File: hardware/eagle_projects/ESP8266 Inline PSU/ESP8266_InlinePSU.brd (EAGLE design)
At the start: 100 x 80 mm, 1 part

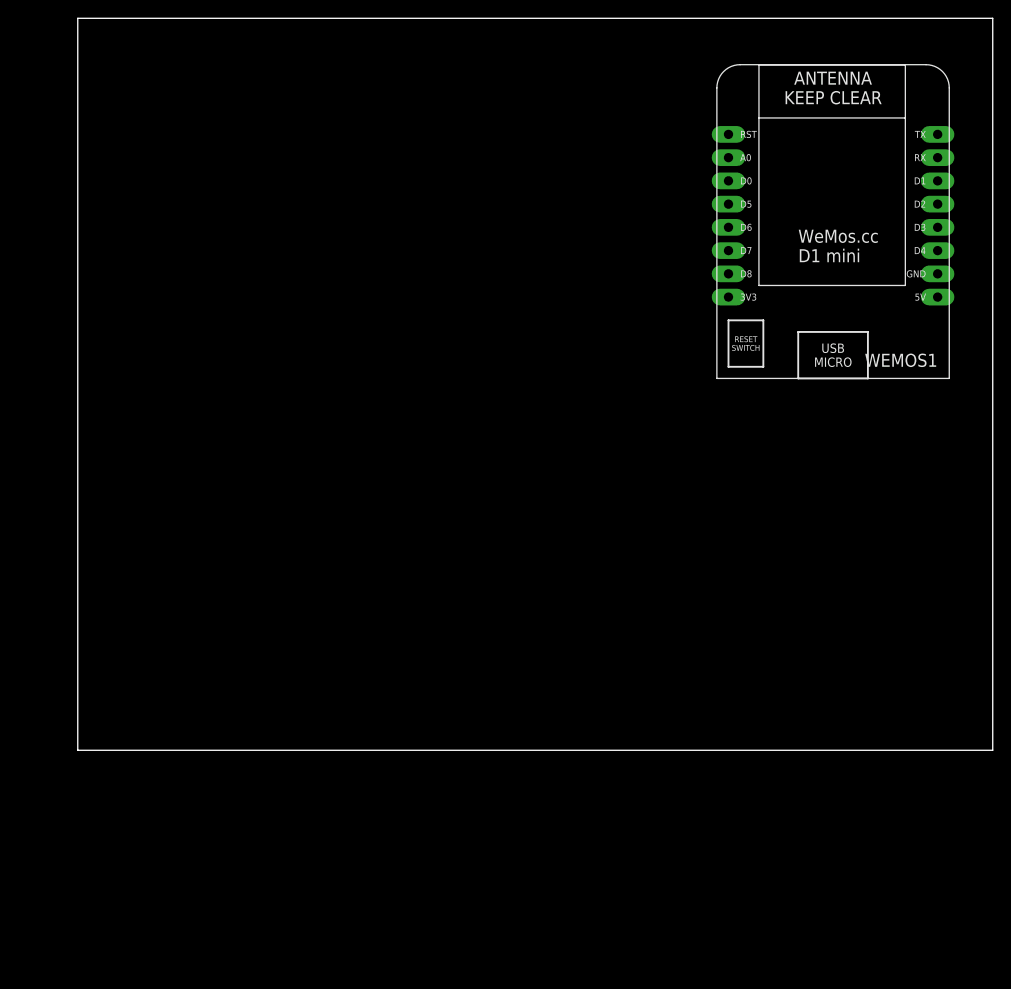
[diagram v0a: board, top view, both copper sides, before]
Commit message: Beginning build process for wireless inline PSU and modifications of PSU
Signed-off-by: Braden Licastro <blicastro@live.com>
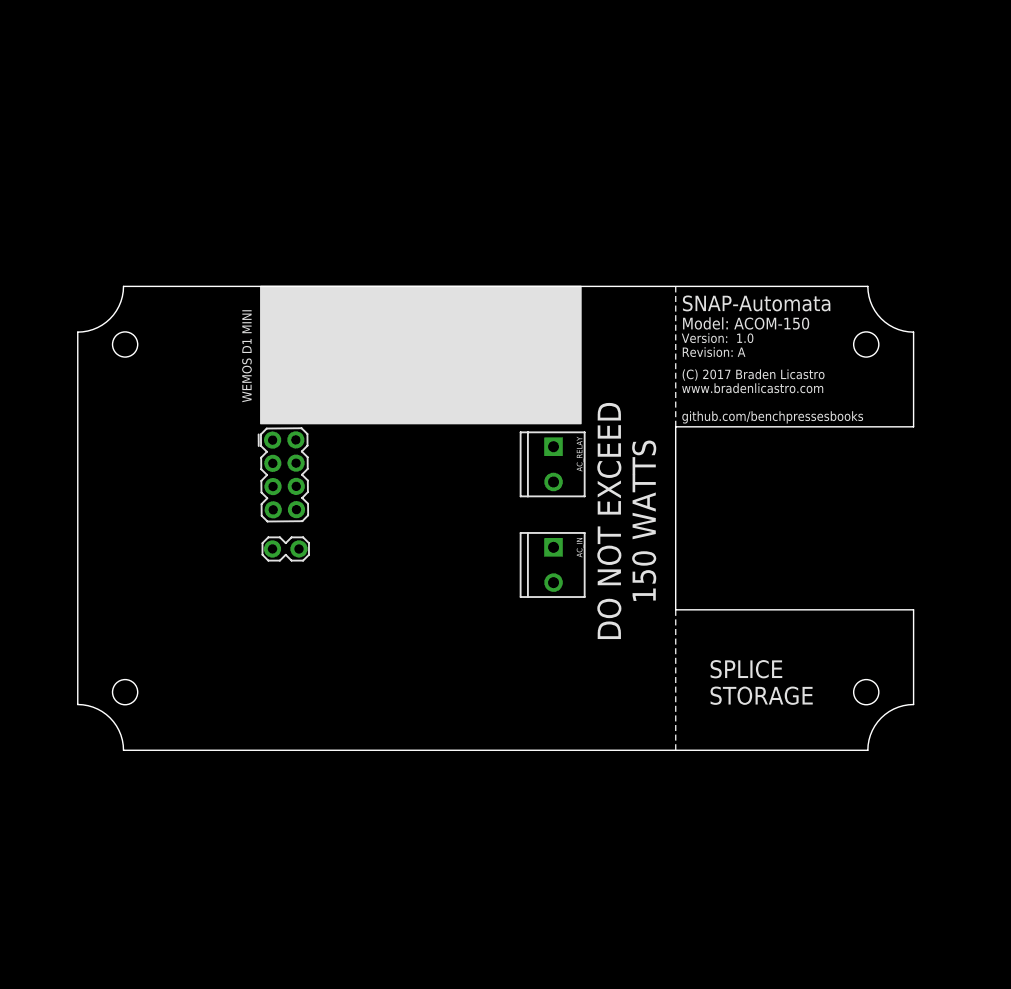
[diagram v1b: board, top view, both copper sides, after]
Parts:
- removed WEMOS1: (no value), esp8266modules:WEMOS-D1-MINI
- added AC_IN, AC_RELAY: (no value), SparkFun-Connectors:SCREWTERMINAL-3.5MM-2_LOCK
- added OVRRD: (no value), SparkFun-Connectors:1X02_LOCK
- added REMOTE_INFC: (no value), SparkFun-Connectors:2X4
- added WEMOS_INFC: (no value), SparkFun-Connectors:2X8
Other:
- board size 100 x 80 mm -> 91.3 x 50.7 mm
- board text added: "(C) 2017 Braden Licastro www.bradenlicastro.com github.com/benchpressesbooks"
- board text added: "DO NOT EXCEED 150 WATTS"
- board text added: "Model: ACOM-150"
- board text added: "SNAP-Automata"
- board text added: "SPLICE STORAGE"
- board text added: "Version: 1.0 Revision: A"
- board text added: "WEMOS D1 MINI"

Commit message: Completed more work on hardware design. Broke out sections of sensitive code, optimised existing code. Hacked new device for use and built new firmware. Updated test firmware for deployment on multiple ESP devices.
Signed-off-by: Braden Licastro <blicastro@live.com>
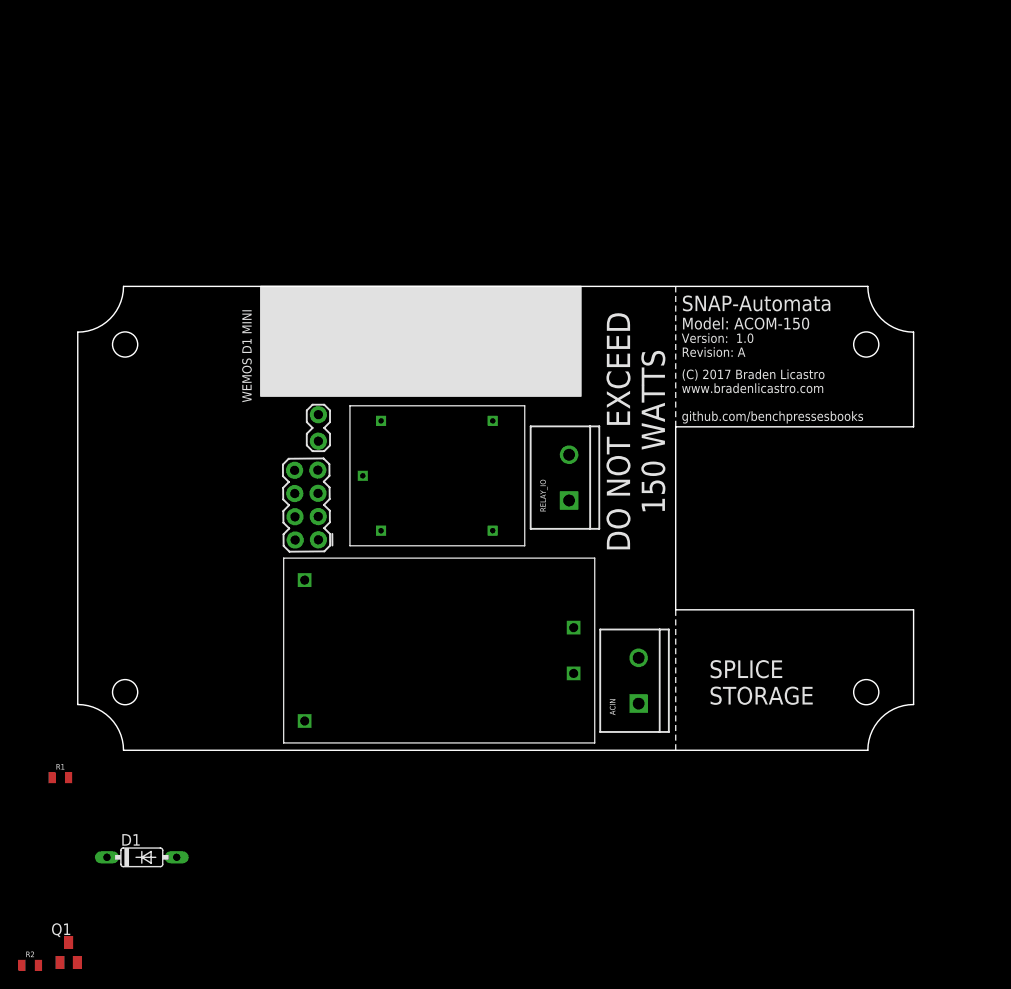
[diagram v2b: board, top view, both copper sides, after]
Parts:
- removed AC_IN, AC_RELAY: (no value), SparkFun-Connectors:SCREWTERMINAL-3.5MM-2_LOCK
- removed WEMOS_INFC: (no value), SparkFun-Connectors:2X8
- added ACIN, RELAY_IO: (no value), SparkFun-Connectors:SCREWTERMINAL-5MM-2
- added D1: 1N4148DO35-7, diode:DO35-7
- added HKLP1: HKLPM01, bl_components:HKLPM01
- added Q1: (no value), semicon-smd-ipc:SOT23
- added R1, R2: (no value), SparkFun-Resistors:0805
- added U$1: SRD-05VDC-SL-CTH, bl_components:SRD-05VDC-SL-C
- added WEMOS_INFC1: (no value), SparkFun-Connectors:2X8
- moved OVRRD 14.7 mm to (26.3, 36.5), turned to 270 degrees
- moved REMOTE_INFC 4.08 mm to (25.0, 26.8), turned to 90.5 degrees
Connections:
- new net N$1: ACIN.2, HKLP1.P$1
- new net N$10: Q1.1, R2.2
- new net N$11: R2.1, WEMOS_INFC1.11
- new net N$2: ACIN.1, HKLP1.P$2
- new net N$3: D1.C, HKLP1.P$4, REMOTE_INFC.1, U$1.P$3, WEMOS_INFC1.1
- new net N$4: OVRRD.1, REMOTE_INFC.2, WEMOS_INFC1.2
- new net N$5: HKLP1.P$3, Q1.2, R1.2, REMOTE_INFC.3, WEMOS_INFC1.3
- new net N$6: RELAY_IO.1, U$1.P$1
- new net N$7: RELAY_IO.2, U$1.P$4
- new net N$8: D1.A, Q1.3, U$1.P$5
- new net N$9: OVRRD.2, R1.1, WEMOS_INFC1.9
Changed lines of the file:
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@@
 <?xml version="1.0" encoding="utf-8"?>
 <!DOCTYPE eagle SYSTEM "eagle.dtd">
-<eagle version="8.4.0">
+<eagle version="8.4.3">
 <drawing>
 <settings>
@@
 <setting verticaltext="up"/>
 </settings>
-<grid distance="1" unitdist="mm" unit="mm" style="lines" multiple="1" display="yes" altdistance="5" altunitdist="mil" altunit="mil"/>
+<grid distance="100" unitdist="mic" unit="mm" style="lines" multiple="1" display="yes" altdistance="5" altunitdist="mil" altunit="mm"/>
 <layers>
 <layer number="1" name="Top" color="4" fill="1" visible="yes" active="yes"/>
@@
 <vertex x="20" y="50.7"/>
 <vertex x="55" y="50.7"/>
-<vertex x="55" y="35.7"/>
-<vertex x="20" y="35.7"/>
+<vertex x="55" y="38.7"/>
+<vertex x="20" y="38.7"/>
 </polygon>
 <text x="19" y="38" size="1.016" layer="21" rot="R90">WEMOS D1 MINI</text>
@@
 www.bradenlicastro.com
 github.com/benchpressesbooks</text>
-<text x="60" y="25" size="2.54" layer="21" rot="R270" align="center">DO NOT EXCEED
+<text x="61" y="34.8" size="2.54" layer="21" rot="R270" align="center">DO NOT EXCEED
 150 WATTS</text>
 </plain>
@@
 <param name="dpMaxLengthDifference" value="10mm"/>
 <param name="dpGapFactor" value="2.5"/>
+<param name="checkAngle" value="0"/>
 <param name="checkFont" value="1"/>
 <param name="checkRestrict" value="0"/>
@@
 </autorouter>
 <elements>
-<element name="WEMOS_INFC" library="SparkFun-Connectors" library_urn="urn:adsk.eagle:library:513" package="2X8" package3d_urn="urn:adsk.eagle:package:38152/1" value="" x="28.888240625" y="46.80739375" smashed="yes">
-<attribute name="VALUE" x="27.618240625" y="44.39439375" size="0.6096" layer="27" font="vector" ratio="20"/>
-</element>
-<element name="REMOTE_INFC" library="SparkFun-Connectors" library_urn="urn:adsk.eagle:library:513" package="2X4" package3d_urn="urn:adsk.eagle:package:38103/1" value="" x="22.6" y="30.1" smashed="yes" rot="R270.5">
-<attribute name="VALUE" x="18.8728125" y="35.14766875" size="0.6096" layer="27" font="vector" ratio="20" rot="R270.5"/>
-</element>
-<element name="OVRRD" library="SparkFun-Connectors" library_urn="urn:adsk.eagle:library:513" package="1X02_LOCK" package3d_urn="urn:adsk.eagle:package:38045/1" value="" x="24" y="22" smashed="yes" rot="R180">
-<attribute name="VALUE" x="25.27" y="24.032" size="0.6096" layer="27" font="vector" ratio="20" rot="R180"/>
-</element>
-<element name="AC_IN" library="SparkFun-Connectors" library_urn="urn:adsk.eagle:library:513" package="SCREWTERMINAL-3.5MM-2_LOCK" package3d_urn="urn:adsk.eagle:package:38049/1" value="" x="52" y="22" rot="R270">
-<attribute name="PROD_ID" value="CONN-08399" x="52" y="22" size="1.016" layer="27" rot="R270" display="off"/>
-</element>
-<element name="AC_RELAY" library="SparkFun-Connectors" library_urn="urn:adsk.eagle:library:513" package="SCREWTERMINAL-3.5MM-2_LOCK" package3d_urn="urn:adsk.eagle:package:38049/1" value="" x="52" y="33" rot="R270">
-<attribute name="PROD_ID" value="CONN-08399" x="52" y="33" size="1.016" layer="27" rot="R270" display="off"/>
+<element name="REMOTE_INFC" library="SparkFun-Connectors" library_urn="urn:adsk.eagle:library:513" package="2X4" package3d_urn="urn:adsk.eagle:package:38103/1" value="" x="25" y="26.8" smashed="yes" rot="R90.5">
+<attribute name="VALUE" x="28.7271875" y="21.75233125" size="0.6096" layer="27" font="vector" ratio="20" rot="R90.5"/>
+</element>
+<element name="OVRRD" library="SparkFun-Connectors" library_urn="urn:adsk.eagle:library:513" package="1X02_LOCK" package3d_urn="urn:adsk.eagle:package:38045/1" value="" x="26.3" y="36.5" smashed="yes" rot="R270">
+<attribute name="VALUE" x="24.268" y="37.77" size="0.6096" layer="27" font="vector" ratio="20" rot="R270"/>
+</element>
+<element name="WEMOS_INFC1" library="SparkFun-Connectors" library_urn="urn:adsk.eagle:library:513" package="2X8" package3d_urn="urn:adsk.eagle:package:38152/1" value="" x="29" y="41"/>
+<element name="HKLP1" library="bl_components" package="HKLPM01" value="HKLPM01" x="39.5" y="10.9" rot="R180"/>
+<element name="U$1" library="bl_components" package="SRD-05VDC-SL-C" value="SRD-05VDC-SL-CTH" x="39.3" y="30"/>
+<element name="RELAY_IO" library="SparkFun-Connectors" library_urn="urn:adsk.eagle:library:513" package="SCREWTERMINAL-5MM-2" package3d_urn="urn:adsk.eagle:package:38044/1" value="" x="53.7" y="27.3" rot="R90">
+<attribute name="SF_SKU" value="PRT-08432" x="53.7" y="27.3" size="1.778" layer="27" rot="R90" display="off"/>
+</element>
+<element name="ACIN" library="SparkFun-Connectors" library_urn="urn:adsk.eagle:library:513" package="SCREWTERMINAL-5MM-2" package3d_urn="urn:adsk.eagle:package:38044/1" value="" x="61.3" y="5.1" rot="R90">
+<attribute name="SF_SKU" value="PRT-08432" x="61.3" y="5.1" size="1.778" layer="27" rot="R90" display="off"/>
+</element>
+<element name="R1" library="SparkFun-Resistors" package="0805" value=" " x="-1.9" y="-3">
+<attribute name="PROD_ID" value=" " x="-1.9" y="-3" size="1.778" layer="27" display="off"/>
+</element>
+<element name="D1" library="diode" library_urn="urn:adsk.eagle:library:210" package="DO35-7" package3d_urn="urn:adsk.eagle:package:43339/1" value="1N4148DO35-7" x="7" y="-11.7"/>
+<element name="Q1" library="semicon-smd-ipc" library_urn="urn:adsk.eagle:library:353" package="SOT23" package3d_urn="urn:adsk.eagle:package:26310/1" value="" x="-1" y="-22.1"/>
+<element name="R2" library="SparkFun-Resistors" package="0805" value=" " x="-5.2" y="-23.5">
+<attribute name="PROD_ID" value=" " x="-5.2" y="-23.5" size="1.778" layer="27" display="off"/>
 </element>
 </elements>
 <signals>
+<signal name="N$1">
+<contactref element="ACIN" pad="2"/>
+<contactref element="HKLP1" pad="P$1"/>
+<wire x1="54.2" y1="8.4" x2="61.3" y2="10.1" width="0" layer="19" extent="1-1"/>
+</signal>
+<signal name="N$2">
+<contactref element="ACIN" pad="1"/>
+<contactref element="HKLP1" pad="P$2"/>
+<wire x1="54.2" y1="13.4" x2="61.3" y2="5.1" width="0" layer="19" extent="1-1"/>
+</signal>
+<signal name="N$3">
+<contactref element="WEMOS_INFC1" pad="1"/>
+<contactref element="REMOTE_INFC" pad="1"/>
+<contactref element="HKLP1" pad="P$4"/>
+<contactref element="U$1" pad="P$3"/>
+<contactref element="D1" pad="C"/>
+<wire x1="33.15" y1="36" x2="29" y2="41" width="0" layer="19" extent="1-1"/>
+<wire x1="26.303196875" y1="23.001225" x2="33.15" y2="36" width="0" layer="19" extent="1-1"/>
+<wire x1="24.8" y1="18.6" x2="26.303196875" y2="23.001225" width="0" layer="19" extent="1-1"/>
+<wire x1="3.19" y1="-11.7" x2="24.8" y2="18.6" width="0" layer="19" extent="1-1"/>
+</signal>
+<signal name="N$4">
+<contactref element="WEMOS_INFC1" pad="2"/>
+<contactref element="REMOTE_INFC" pad="2"/>
+<contactref element="OVRRD" pad="1"/>
+<wire x1="26.3" y1="36.6778" x2="29" y2="43.54" width="0" layer="19" extent="1-1"/>
+<wire x1="23.76329375" y1="22.979059375" x2="26.3" y2="36.6778" width="0" layer="19" extent="1-1"/>
+</signal>
+<signal name="N$5">
+<contactref element="WEMOS_INFC1" pad="3"/>
+<contactref element="REMOTE_INFC" pad="3"/>
+<contactref element="HKLP1" pad="P$3"/>
+<contactref element="R1" pad="2"/>
+<contactref element="Q1" pad="2"/>
+<wire x1="26.28103125" y1="25.541128125" x2="31.54" y2="41" width="0" layer="19" extent="1-1"/>
+<wire x1="24.8" y1="3.2" x2="26.28103125" y2="25.541128125" width="0" layer="19" extent="1-1"/>
+<wire x1="-1" y1="-3" x2="24.8" y2="3.2" width="0" layer="19" extent="1-1"/>
+<wire x1="-0.05" y1="-23.2" x2="-1" y2="-3" width="0" layer="19" extent="1-1"/>
+</signal>
+<signal name="N$9">
+<contactref element="OVRRD" pad="2"/>
+<contactref element="WEMOS_INFC1" pad="9"/>
+<contactref element="R1" pad="1"/>
+<wire x1="26.3" y1="33.7822" x2="39.16" y2="41" width="0" layer="19" extent="1-1"/>
+<wire x1="-2.8" y1="-3" x2="26.3" y2="33.7822" width="0" layer="19" extent="1-1"/>
+</signal>
+<signal name="N$6">
+<contactref element="RELAY_IO" pad="1"/>
+<contactref element="U$1" pad="P$1"/>
+<wire x1="45.35" y1="36" x2="53.7" y2="27.3" width="0" layer="19" extent="1-1"/>
+</signal>
+<signal name="N$7">
+<contactref element="U$1" pad="P$4"/>
+<contactref element="RELAY_IO" pad="2"/>
+<wire x1="31.15" y1="30" x2="53.7" y2="32.3" width="0" layer="19" extent="1-1"/>
+</signal>
+<signal name="N$8">
+<contactref element="U$1" pad="P$5"/>
+<contactref element="D1" pad="A"/>
+<contactref element="Q1" pad="3"/>
+<wire x1="10.81" y1="-11.7" x2="33.15" y2="24" width="0" layer="19" extent="1-1"/>
+<wire x1="-1" y1="-21" x2="10.81" y2="-11.7" width="0" layer="19" extent="1-1"/>
+</signal>
+<signal name="N$10">
+<contactref element="Q1" pad="1"/>
+<contactref element="R2" pad="2"/>
+<wire x1="-1.95" y1="-23.2" x2="-4.3" y2="-23.5" width="0" layer="19" extent="1-1"/>
+</signal>
+<signal name="N$11">
+<contactref element="R2" pad="1"/>
+<contactref element="WEMOS_INFC1" pad="11"/>
+<wire x1="-6.1" y1="-23.5" x2="41.7" y2="41" width="0" layer="19" extent="1-1"/>
+</signal>
 </signals>
 </board>
